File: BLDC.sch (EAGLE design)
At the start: 131 parts, among them J1 JST-1X7-MICRO, J2 JST-1X7-MICRO, J4 IPBT-102-H1-XX-S-RA, J5 IPBT-103-H1-XX-S-RA, J6 JST-1X7-MICRO, J7 JST-1X7-MICRO, J8 JST-1X7-MICRO, Q1 IRFS7530TRLPBF, Q2 IRFS7530TRLPBF, Q3 IRFS7530TRLPBF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

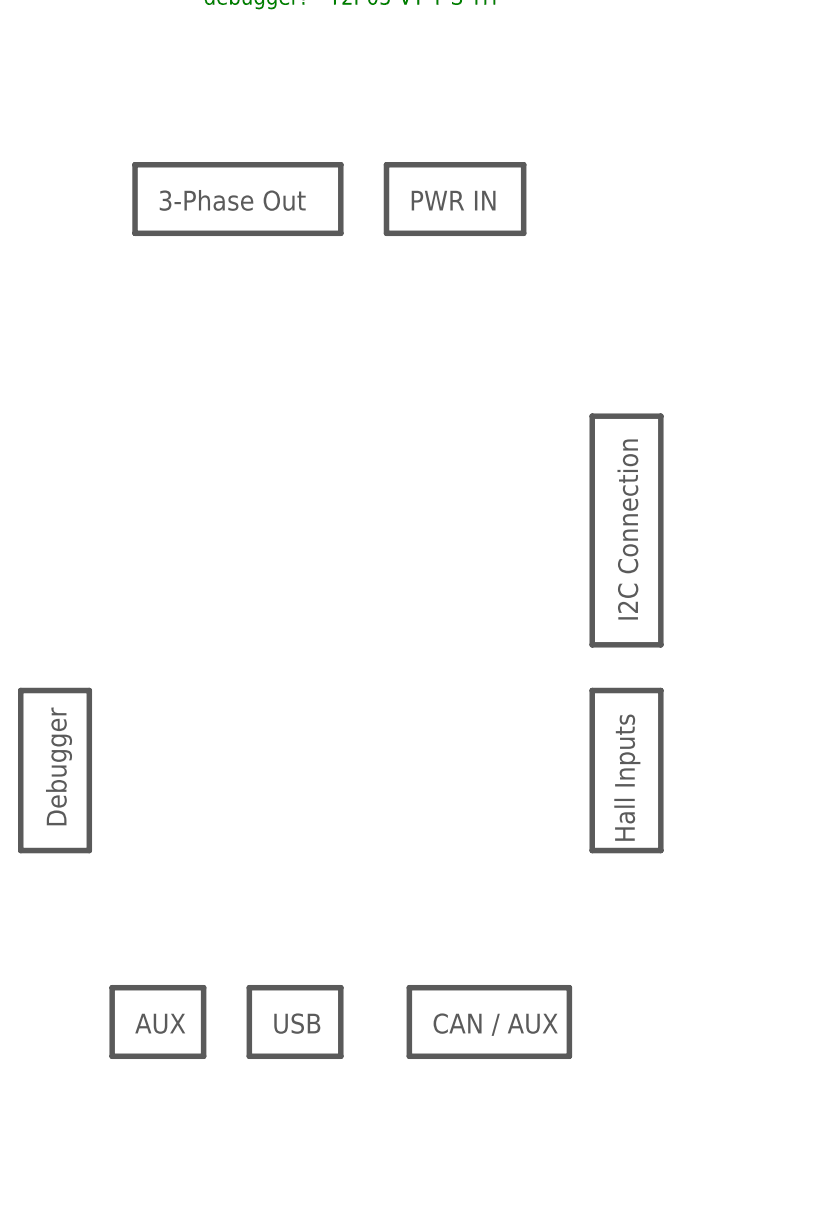
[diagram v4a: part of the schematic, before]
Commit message: placed usb connect
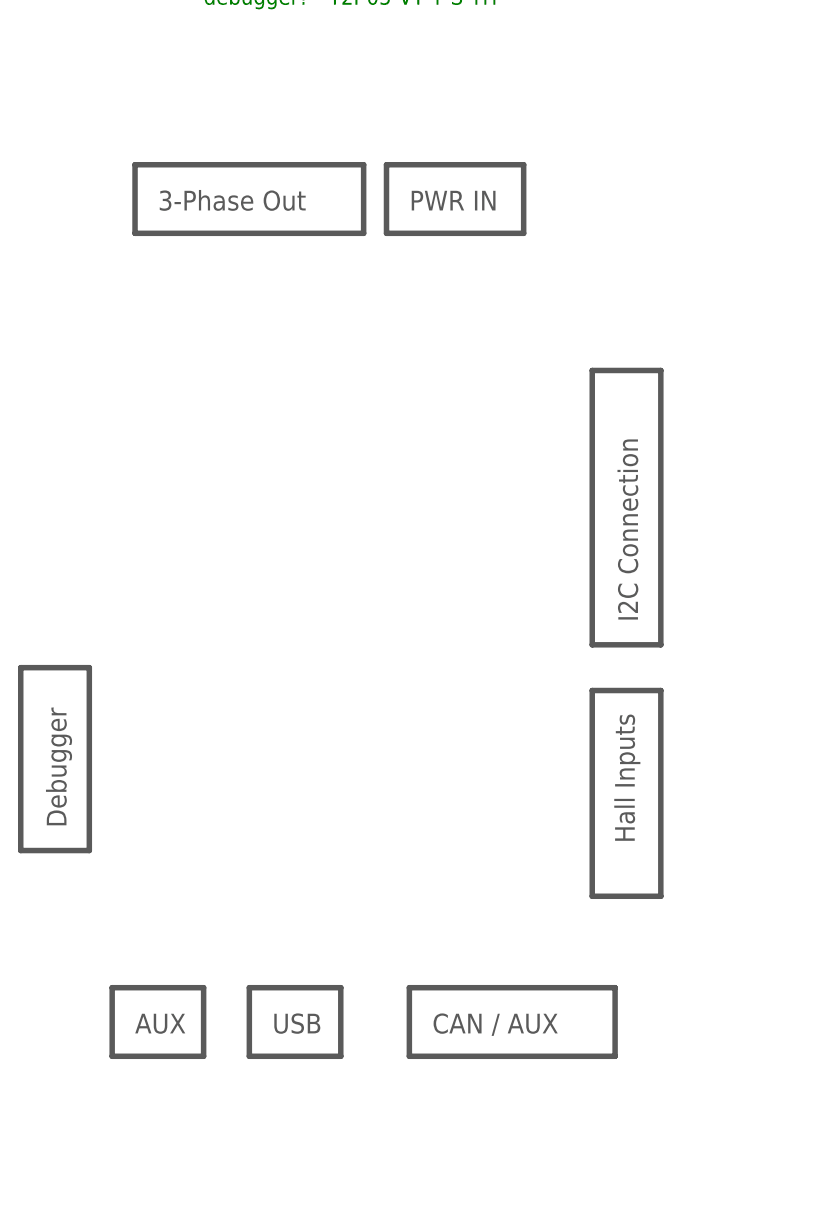
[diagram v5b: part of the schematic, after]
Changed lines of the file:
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@@
 <wire x1="-447.04" y1="10.16" x2="-457.2" y2="10.16" width="0.6096" layer="97"/>
 <wire x1="-457.2" y1="10.16" x2="-457.2" y2="17.78" width="0.6096" layer="97"/>
-<wire x1="-439.42" y1="17.78" x2="-421.64" y2="17.78" width="0.6096" layer="97"/>
-<wire x1="-421.64" y1="17.78" x2="-421.64" y2="10.16" width="0.6096" layer="97"/>
-<wire x1="-421.64" y1="10.16" x2="-439.42" y2="10.16" width="0.6096" layer="97"/>
+<wire x1="-439.42" y1="17.78" x2="-416.56" y2="17.78" width="0.6096" layer="97"/>
+<wire x1="-416.56" y1="17.78" x2="-416.56" y2="10.16" width="0.6096" layer="97"/>
+<wire x1="-416.56" y1="10.16" x2="-439.42" y2="10.16" width="0.6096" layer="97"/>
 <wire x1="-439.42" y1="10.16" x2="-439.42" y2="17.78" width="0.6096" layer="97"/>
-<wire x1="-482.6" y1="33.02" x2="-482.6" y2="50.8" width="0.6096" layer="97"/>
-<wire x1="-482.6" y1="50.8" x2="-474.98" y2="50.8" width="0.6096" layer="97"/>
-<wire x1="-474.98" y1="50.8" x2="-474.98" y2="33.02" width="0.6096" layer="97"/>
+<wire x1="-482.6" y1="33.02" x2="-482.6" y2="53.34" width="0.6096" layer="97"/>
+<wire x1="-482.6" y1="53.34" x2="-474.98" y2="53.34" width="0.6096" layer="97"/>
+<wire x1="-474.98" y1="53.34" x2="-474.98" y2="33.02" width="0.6096" layer="97"/>
 <wire x1="-474.98" y1="33.02" x2="-482.6" y2="33.02" width="0.6096" layer="97"/>
-<wire x1="-411.48" y1="50.8" x2="-411.48" y2="33.02" width="0.6096" layer="97"/>
-<wire x1="-411.48" y1="33.02" x2="-419.1" y2="33.02" width="0.6096" layer="97"/>
-<wire x1="-419.1" y1="33.02" x2="-419.1" y2="50.8" width="0.6096" layer="97"/>
+<wire x1="-411.48" y1="50.8" x2="-411.48" y2="27.94" width="0.6096" layer="97"/>
+<wire x1="-411.48" y1="27.94" x2="-419.1" y2="27.94" width="0.6096" layer="97"/>
+<wire x1="-419.1" y1="27.94" x2="-419.1" y2="50.8" width="0.6096" layer="97"/>
 <wire x1="-419.1" y1="50.8" x2="-411.48" y2="50.8" width="0.6096" layer="97"/>
-<wire x1="-419.1" y1="55.88" x2="-419.1" y2="81.28" width="0.6096" layer="97"/>
-<wire x1="-419.1" y1="81.28" x2="-411.48" y2="81.28" width="0.6096" layer="97"/>
-<wire x1="-411.48" y1="81.28" x2="-411.48" y2="55.88" width="0.6096" layer="97"/>
+<wire x1="-419.1" y1="55.88" x2="-419.1" y2="86.36" width="0.6096" layer="97"/>
+<wire x1="-419.1" y1="86.36" x2="-411.48" y2="86.36" width="0.6096" layer="97"/>
+<wire x1="-411.48" y1="86.36" x2="-411.48" y2="55.88" width="0.6096" layer="97"/>
 <wire x1="-411.48" y1="55.88" x2="-419.1" y2="55.88" width="0.6096" layer="97"/>
 <text x="-439.42" y="104.14" size="2.1844" layer="97">PWR IN</text>
@@
 <wire x1="-441.96" y1="101.6" x2="-441.96" y2="109.22" width="0.6096" layer="97"/>
 <text x="-467.36" y="104.14" size="2.1844" layer="97">3-Phase Out</text>
-<wire x1="-469.9" y1="109.22" x2="-447.04" y2="109.22" width="0.6096" layer="97"/>
-<wire x1="-447.04" y1="109.22" x2="-447.04" y2="101.6" width="0.6096" layer="97"/>
-<wire x1="-447.04" y1="101.6" x2="-469.9" y2="101.6" width="0.6096" layer="97"/>
+<wire x1="-469.9" y1="109.22" x2="-444.5" y2="109.22" width="0.6096" layer="97"/>
+<wire x1="-444.5" y1="109.22" x2="-444.5" y2="101.6" width="0.6096" layer="97"/>
+<wire x1="-444.5" y1="101.6" x2="-469.9" y2="101.6" width="0.6096" layer="97"/>
 <wire x1="-469.9" y1="101.6" x2="-469.9" y2="109.22" width="0.6096" layer="97"/>
 </plain>

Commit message: rough layout of all component groups done
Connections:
- removed net V_BATT: R12.1
- net VCC: now also R12.1
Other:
- note added: "Put close to big fets"
- note removed: "where to put?"
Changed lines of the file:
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@@
 <wire x1="-304.8" y1="-147.32" x2="-337.82" y2="-147.32" width="0.6096" layer="97"/>
 <wire x1="-337.82" y1="-147.32" x2="-337.82" y2="-58.42" width="0.6096" layer="97"/>
-<text x="-45.72" y="-86.36" size="6.4516" layer="97">where to put?</text>
 <text x="-114.3" y="-76.2" size="5.08" layer="97">STM32 LEDS</text>
 <wire x1="-119.38" y1="-68.58" x2="-63.5" y2="-68.58" width="0.6096" layer="97"/>
@@
 <wire x1="-119.38" y1="-129.54" x2="-119.38" y2="-68.58" width="0.6096" layer="97"/>
 <text x="-238.76" y="58.42" size="2.1844" layer="97">I2C Connection</text>
-<text x="-414.02" y="58.42" size="2.1844" layer="97" rot="R90">I2C Connection</text>
+<text x="-393.7" y="63.5" size="2.1844" layer="97" rot="R90">I2C Connection</text>
 <text x="-276.86" y="-35.56" size="2.1844" layer="97" rot="R270">CAN / AUX</text>
 <text x="-436.88" y="12.7" size="2.1844" layer="97">CAN / AUX</text>
 <text x="-276.86" y="5.08" size="2.1844" layer="97" rot="R270">AUX</text>
-<text x="-469.9" y="12.7" size="2.1844" layer="97">AUX</text>
+<text x="-485.14" y="40.64" size="2.1844" layer="97" rot="R270">AUX</text>
 <text x="-264.16" y="106.68" size="2.1844" layer="97">USB</text>
 <text x="-454.66" y="12.7" size="2.1844" layer="97">USB</text>
-<text x="-477.52" y="35.56" size="2.1844" layer="97" rot="R90">Debugger</text>
-<text x="-416.56" y="48.26" size="2.1844" layer="97" rot="R270">Hall Inputs</text>
+<text x="-396.24" y="50.8" size="2.1844" layer="97" rot="R270">Debugger</text>
+<text x="-462.28" y="15.24" size="2.1844" layer="97" rot="R180">Hall Inputs</text>
 <text x="-279.4" y="50.8" size="2.1844" layer="97" rot="R90">Hall Inputs</text>
-<wire x1="-472.44" y1="17.78" x2="-462.28" y2="17.78" width="0.6096" layer="97"/>
-<wire x1="-462.28" y1="17.78" x2="-462.28" y2="10.16" width="0.6096" layer="97"/>
-<wire x1="-462.28" y1="10.16" x2="-472.44" y2="10.16" width="0.6096" layer="97"/>
-<wire x1="-472.44" y1="10.16" x2="-472.44" y2="17.78" width="0.6096" layer="97"/>
+<wire x1="-480.06" y1="43.18" x2="-480.06" y2="33.02" width="0.6096" layer="97"/>
+<wire x1="-480.06" y1="33.02" x2="-487.68" y2="33.02" width="0.6096" layer="97"/>
+<wire x1="-487.68" y1="33.02" x2="-487.68" y2="43.18" width="0.6096" layer="97"/>
+<wire x1="-487.68" y1="43.18" x2="-480.06" y2="43.18" width="0.6096" layer="97"/>
 <wire x1="-457.2" y1="17.78" x2="-447.04" y2="17.78" width="0.6096" layer="97"/>
 <wire x1="-447.04" y1="17.78" x2="-447.04" y2="10.16" width="0.6096" layer="97"/>
@@
 <wire x1="-416.56" y1="10.16" x2="-439.42" y2="10.16" width="0.6096" layer="97"/>
 <wire x1="-439.42" y1="10.16" x2="-439.42" y2="17.78" width="0.6096" layer="97"/>
-<wire x1="-482.6" y1="33.02" x2="-482.6" y2="53.34" width="0.6096" layer="97"/>
-<wire x1="-482.6" y1="53.34" x2="-474.98" y2="53.34" width="0.6096" layer="97"/>
-<wire x1="-474.98" y1="53.34" x2="-474.98" y2="33.02" width="0.6096" layer="97"/>
-<wire x1="-474.98" y1="33.02" x2="-482.6" y2="33.02" width="0.6096" layer="97"/>
-<wire x1="-411.48" y1="50.8" x2="-411.48" y2="27.94" width="0.6096" layer="97"/>
-<wire x1="-411.48" y1="27.94" x2="-419.1" y2="27.94" width="0.6096" layer="97"/>
-<wire x1="-419.1" y1="27.94" x2="-419.1" y2="50.8" width="0.6096" layer="97"/>
-<wire x1="-419.1" y1="50.8" x2="-411.48" y2="50.8" width="0.6096" layer="97"/>
-<wire x1="-419.1" y1="55.88" x2="-419.1" y2="86.36" width="0.6096" layer="97"/>
-<wire x1="-419.1" y1="86.36" x2="-411.48" y2="86.36" width="0.6096" layer="97"/>
-<wire x1="-411.48" y1="86.36" x2="-411.48" y2="55.88" width="0.6096" layer="97"/>
-<wire x1="-411.48" y1="55.88" x2="-419.1" y2="55.88" width="0.6096" layer="97"/>
+<wire x1="-391.16" y1="53.34" x2="-391.16" y2="33.02" width="0.6096" layer="97"/>
+<wire x1="-391.16" y1="33.02" x2="-398.78" y2="33.02" width="0.6096" layer="97"/>
+<wire x1="-398.78" y1="33.02" x2="-398.78" y2="53.34" width="0.6096" layer="97"/>
+<wire x1="-398.78" y1="53.34" x2="-391.16" y2="53.34" width="0.6096" layer="97"/>
+<wire x1="-459.74" y1="10.16" x2="-482.6" y2="10.16" width="0.6096" layer="97"/>
+<wire x1="-482.6" y1="10.16" x2="-482.6" y2="17.78" width="0.6096" layer="97"/>
+<wire x1="-482.6" y1="17.78" x2="-459.74" y2="17.78" width="0.6096" layer="97"/>
+<wire x1="-459.74" y1="17.78" x2="-459.74" y2="10.16" width="0.6096" layer="97"/>
+<wire x1="-398.78" y1="60.96" x2="-398.78" y2="91.44" width="0.6096" layer="97"/>
+<wire x1="-398.78" y1="91.44" x2="-391.16" y2="91.44" width="0.6096" layer="97"/>
+<wire x1="-391.16" y1="91.44" x2="-391.16" y2="60.96" width="0.6096" layer="97"/>
+<wire x1="-391.16" y1="60.96" x2="-398.78" y2="60.96" width="0.6096" layer="97"/>
 <text x="-439.42" y="104.14" size="2.1844" layer="97">PWR IN</text>
 <wire x1="-441.96" y1="109.22" x2="-426.72" y2="109.22" width="0.6096" layer="97"/>
@@
 <wire x1="-444.5" y1="101.6" x2="-469.9" y2="101.6" width="0.6096" layer="97"/>
 <wire x1="-469.9" y1="101.6" x2="-469.9" y2="109.22" width="0.6096" layer="97"/>
+<text x="-12.7" y="-71.12" size="1.778" layer="91">Put close to big fets</text>
 </plain>
 <instances>
@@
 </segment>
 </net>
-<net name="V_BATT" class="0">
-<segment>
-<pinref part="R12" gate="G$1" pin="1"/>
-<wire x1="-121.92" y1="129.54" x2="-121.92" y2="132.08" width="0.1524" layer="91"/>
-<wire x1="-121.92" y1="132.08" x2="-124.46" y2="132.08" width="0.1524" layer="91"/>
-<label x="-124.46" y="132.08" size="1.778" layer="95" rot="R180" xref="yes"/>
-</segment>
-</net>
 <net name="AN_IN" class="0">
 <segment>
@@
 <wire x1="-218.44" y1="-17.78" x2="-220.98" y2="-17.78" width="0.1524" layer="91"/>
 </segment>
-</net>
+<segment>
+<pinref part="R12" gate="G$1" pin="1"/>
+<wire x1="-121.92" y1="129.54" x2="-121.92" y2="132.08" width="0.1524" layer="91"/>
+<wire x1="-121.92" y1="132.08" x2="-124.46" y2="132.08" width="0.1524" layer="91"/>
+<label x="-124.46" y="132.08" size="1.778" layer="95" rot="R180" xref="yes"/>
+</segment>
+</net>

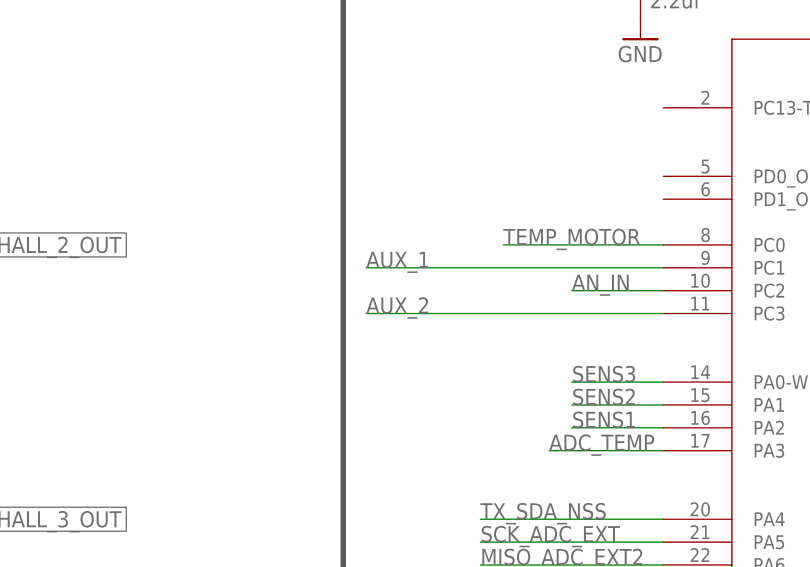
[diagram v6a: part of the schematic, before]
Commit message: final board dimentions defined
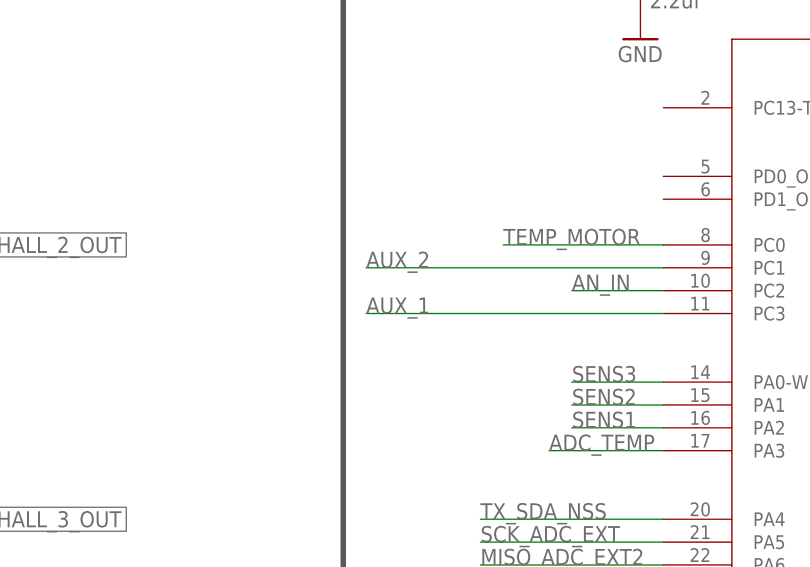
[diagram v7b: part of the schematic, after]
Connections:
- net AUX_1: now also U2.PC3; no longer U2.PC1
- net AUX_2: now also U2.PC1; no longer U2.PC3
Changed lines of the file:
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@@
-</segment>
-<segment>
-<pinref part="U2" gate="A" pin="PC1"/>
-<wire x1="-55.88" y1="17.78" x2="-88.9" y2="17.78" width="0.1524" layer="91"/>
-<label x="-88.9" y="17.78" size="1.778" layer="95"/>
 </segment>
 <segment>
@@
 <wire x1="-322.58" y1="-83.82" x2="-332.74" y2="-83.82" width="0.1524" layer="91"/>
 <label x="-332.74" y="-83.82" size="1.778" layer="95"/>
+</segment>
+<segment>
+<pinref part="U2" gate="A" pin="PC3"/>
+<wire x1="-55.88" y1="12.7" x2="-88.9" y2="12.7" width="0.1524" layer="91"/>
+<label x="-88.9" y="12.7" size="1.778" layer="95"/>
 </segment>
 </net>
@@
 </segment>
 <segment>
-<pinref part="U2" gate="A" pin="PC3"/>
-<wire x1="-55.88" y1="12.7" x2="-88.9" y2="12.7" width="0.1524" layer="91"/>
-<label x="-88.9" y="12.7" size="1.778" layer="95"/>
-</segment>
-<segment>
 <pinref part="R47" gate="G$1" pin="2"/>
 <wire x1="-322.58" y1="-91.44" x2="-332.74" y2="-91.44" width="0.1524" layer="91"/>
 <label x="-332.74" y="-91.44" size="1.778" layer="95"/>
 </segment>
+<segment>
+<pinref part="U2" gate="A" pin="PC1"/>
+<wire x1="-55.88" y1="17.78" x2="-88.9" y2="17.78" width="0.1524" layer="91"/>
+<label x="-88.9" y="17.78" size="1.778" layer="95"/>
+</segment>
 </net>

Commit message: added jumper so H2_LOW doesn't connect directly to GND b/c Im paranoid
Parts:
- removed C1: 2200uF, FormE:UVR1J222MHD
- added C49: 2200uF, FormE:UVR1J222MHD
- added R54: 0k, adafruit:R-US_R0805
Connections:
- new net H2_LOW: Q4.S, R42.2, R54.2, U3.SL_B
- net +3V3: now also J6.2; no longer J6.6
- net +5V: now also J6.1; no longer J6.7
- net DGND: now also C49.-, J4.2; no longer C1.-, J4.1
- net GND: now also J6.7, J7.7, R54.1; no longer J6.1, J7.2, Q4.S, R42.2, U3.SL_B
- net MISO_ADC_EXT2: now also J6.3; no longer J6.2
- net M_L1: no longer R43.1
- net M_L3: now also R43.1
- net SCK_ADC_EXT: now also J6.4; no longer J6.3
- net SWCLK: now also J7.2; no longer J7.5
- net SWDIO: now also J7.1; no longer J7.4
- net TX_SDA_NSS: now also J6.6; no longer J6.4
- net VCC: now also C49.+, J4.1; no longer C1.+, J4.2
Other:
- moved on the sheet: J4, R35
